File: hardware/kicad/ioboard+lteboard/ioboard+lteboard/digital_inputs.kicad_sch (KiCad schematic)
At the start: 35 parts, among them J2 Conn_01x09, U6 LTV-247, U7 LTV-247

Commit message: added missing hierarchical labels for core-compute, digitil_inputs and relay_output
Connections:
- net DI4_MCU: now reaches C7.2, R15.1, U7.10
- net DI2_MCU: now reaches C3.2, R7.1, U7.14
- net DI6_MCU: now reaches C1.2, R5.1, U6.14
- net DI7_MCU: now reaches C6.2, R14.1, U6.12
- net DI5_MCU: now reaches C2.2, R6.1, U6.16
- net DI1_MCU: now reaches C4.2, R8.1, U7.16
- net DI3_MCU: now reaches C8.2, R16.1, U7.12
- net DI8_MCU: now reaches C5.2, R13.1, U6.10
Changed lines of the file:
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@@
+	(wire
+		(pts
+			(xy 83.82 36.83) (xy 81.28 36.83)
+		)
+		(stroke
+			(width 0)
+			(type default)
+		)
+	)
 	(wire
 		(pts
@@
 	(wire
 		(pts
+			(xy 152.4 36.83) (xy 149.86 36.83)
+		)
+		(stroke
+			(width 0)
+			(type default)
+		)
+	)
+	(wire
+		(pts
 			(xy 96.52 166.37) (xy 109.22 166.37)
 		)
@@
 	(wire
 		(pts
+			(xy 148.59 161.29) (xy 146.05 161.29)
+		)
+		(stroke
+			(width 0)
+			(type default)
+		)
+	)
+	(wire
+		(pts
 			(xy 100.33 41.91) (xy 113.03 41.91)
 		)
@@
 	(wire
 		(pts
+			(xy 80.01 161.29) (xy 77.47 161.29)
+		)
+		(stroke
+			(width 0)
+			(type default)
+		)
+	)
+	(wire
+		(pts
 			(xy 191.77 81.28) (xy 204.47 81.28)
 		)
@@
 	(wire
 		(pts
+			(xy 81.28 120.65) (xy 78.74 120.65)
+		)
+		(stroke
+			(width 0)
+			(type default)
+		)
+	)
+	(wire
+		(pts
 			(xy 119.38 82.55) (xy 125.73 82.55)
 		)
@@
 	(wire
 		(pts
+			(xy 151.13 77.47) (xy 148.59 77.47)
+		)
+		(stroke
+			(width 0)
+			(type default)
+		)
+	)
+	(wire
+		(pts
+			(xy 149.86 120.65) (xy 147.32 120.65)
+		)
+		(stroke
+			(width 0)
+			(type default)
+		)
+	)
+	(wire
+		(pts
 			(xy 73.66 82.55) (xy 72.39 82.55)
 		)
@@
 		(pts
 			(xy 35.56 120.65) (xy 41.91 120.65)
+		)
+		(stroke
+			(width 0)
+			(type default)
+		)
+	)
+	(wire
+		(pts
+			(xy 82.55 77.47) (xy 80.01 77.47)
 		)
 		(stroke
@@
 	)
 	(label "DI5_IN"
-		(at 191.77 88.9 0)
+		(at 194.31 88.9 0)
 		(effects
 			(font
@@
 	)
 	(label "DI8_IN"
-		(at 191.77 96.52 0)
+		(at 194.31 96.52 0)
 		(effects
 			(font
@@
 	)
 	(label "DI1_IN"
-		(at 191.77 78.74 0)
+		(at 194.31 78.74 0)
 		(effects
 			(font
@@
 	)
 	(label "DI7_IN"
-		(at 191.77 93.98 0)
+		(at 194.31 93.98 0)
 		(effects
 			(font
@@
 	)
 	(label "DI3_IN"
-		(at 191.77 83.82 0)
+		(at 194.31 83.82 0)
 		(effects
 			(font
@@
 	)
 	(label "DI6_IN"
-		(at 191.77 91.44 0)
+		(at 194.31 91.44 0)
 		(effects
 			(font
@@
 	)
 	(label "DI2_IN"
-		(at 191.77 81.28 0)
+		(at 194.31 81.28 0)
 		(effects
 			(font
@@
 	)
 	(label "DI4_IN"
-		(at 191.77 86.36 0)
+		(at 194.31 86.36 0)
 		(effects
 			(font
@@
 		)
 	)
+	(hierarchical_label "DI8_MCU"
+		(shape output)
+		(at 148.59 161.29 0)
+		(effects
+			(font
+				(size 1.27 1.27)
+			)
+			(justify left)
+		)
+	)
 	(hierarchical_label "3V3_LOGIC"
 		(shape input)
@@
 		)
 	)
+	(hierarchical_label "DI4_MCU"
+		(shape output)
+		(at 151.13 77.47 0)
+		(effects
+			(font
+				(size 1.27 1.27)
+			)
+			(justify left)
+		)
+	)
+	(hierarchical_label "DI2_MCU"
+		(shape output)
+		(at 82.55 77.47 0)
+		(effects
+			(font
+				(size 1.27 1.27)
+			)
+			(justify left)
+		)
+	)
+	(hierarchical_label "DI1_MCU"
+		(shape output)
+		(at 83.82 36.83 0)
+		(effects
+			(font
+				(size 1.27 1.27)
+			)
+			(justify left)
+		)
+	)
+	(hierarchical_label "DI6_MCU"
+		(shape output)
+		(at 80.01 161.29 0)
+		(effects
+			(font
+				(size 1.27 1.27)
+			)
+			(justify left)
+		)
+	)
 	(hierarchical_label "3V3_LOGIC"
 		(shape input)
@@
 		(effects
 			(font
+				(size 1.27 1.27)
+			)
+			(justify left)
+		)
+	)
+	(hierarchical_label "DI5_MCU"
+		(shape output)
+		(at 81.28 120.65 0)
+		(effects
+			(font
+				(size 1.27 1.27)
+			)
+			(justify left)
+		)
+	)
+	(hierarchical_label "DI3_MCU"
+		(shape output)
+		(at 152.4 36.83 0)
+		(effects
+			(font
+				(size 1.27 1.27)
+			)
+			(justify left)
+		)
+	)
+	(hierarchical_label "DI7_MCU"
+		(shape output)
+		(at 149.86 120.65 0)
+		(effects
+			(font

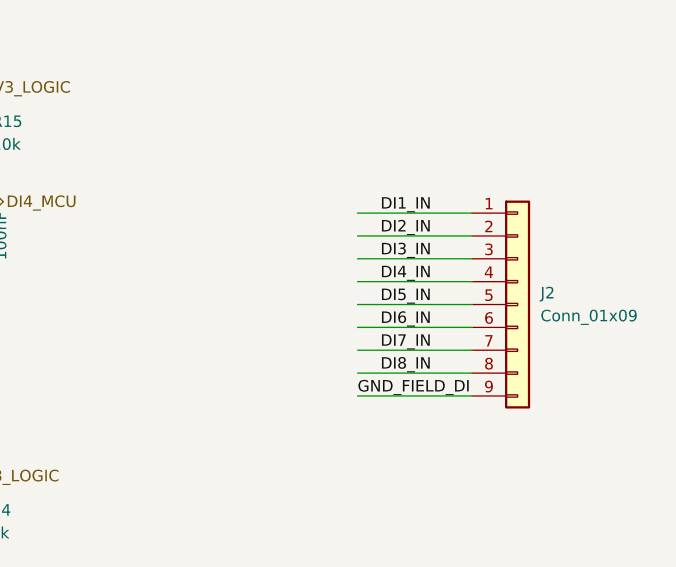
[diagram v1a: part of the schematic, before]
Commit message: Close roadmap steps 6/7: pin assignment, board-to-board wiring, ERC pass clean; update docs to match
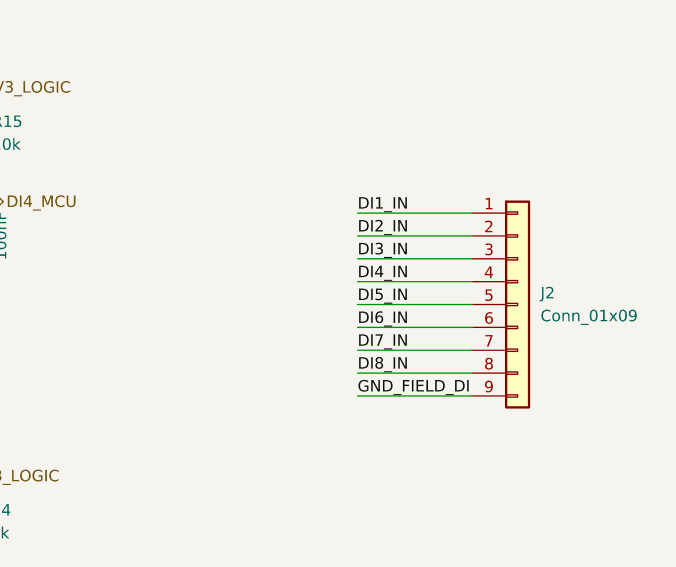
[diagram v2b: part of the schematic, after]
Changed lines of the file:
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@@
 	)
 	(label "DI5_IN"
-		(at 194.31 88.9 0)
+		(at 191.77 88.9 0)
 		(effects
 			(font
@@
 	)
 	(label "DI8_IN"
-		(at 194.31 96.52 0)
+		(at 191.77 96.52 0)
 		(effects
 			(font
@@
 	)
 	(label "DI1_IN"
-		(at 194.31 78.74 0)
+		(at 191.77 78.74 0)
 		(effects
 			(font
@@
 	)
 	(label "DI7_IN"
-		(at 194.31 93.98 0)
+		(at 191.77 93.98 0)
 		(effects
 			(font
@@
 	)
 	(label "DI3_IN"
-		(at 194.31 83.82 0)
+		(at 191.77 83.82 0)
 		(effects
 			(font
@@
 	)
 	(label "DI6_IN"
-		(at 194.31 91.44 0)
+		(at 191.77 91.44 0)
 		(effects
 			(font
@@
 	)
 	(label "DI2_IN"
-		(at 194.31 81.28 0)
+		(at 191.77 81.28 0)
 		(effects
 			(font
@@
 	)
 	(label "DI4_IN"
-		(at 194.31 86.36 0)
+		(at 191.77 86.36 0)
 		(effects
 			(font
